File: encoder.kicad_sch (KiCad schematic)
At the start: 24 parts

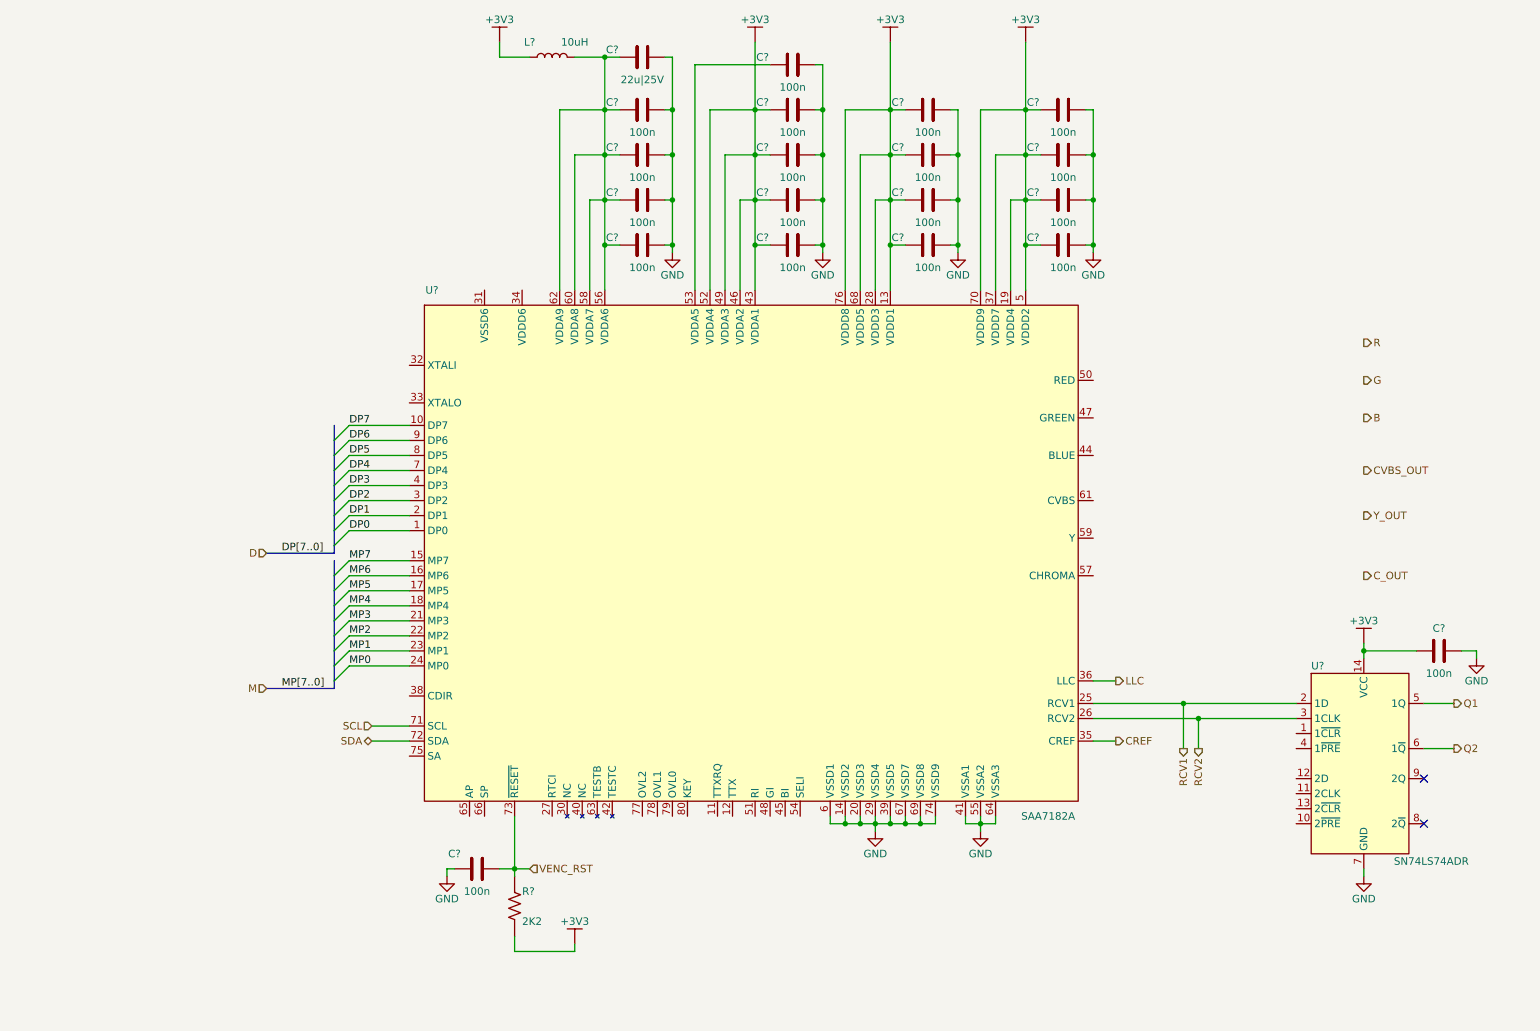
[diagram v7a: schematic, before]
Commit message: added connectors and crystal, osc
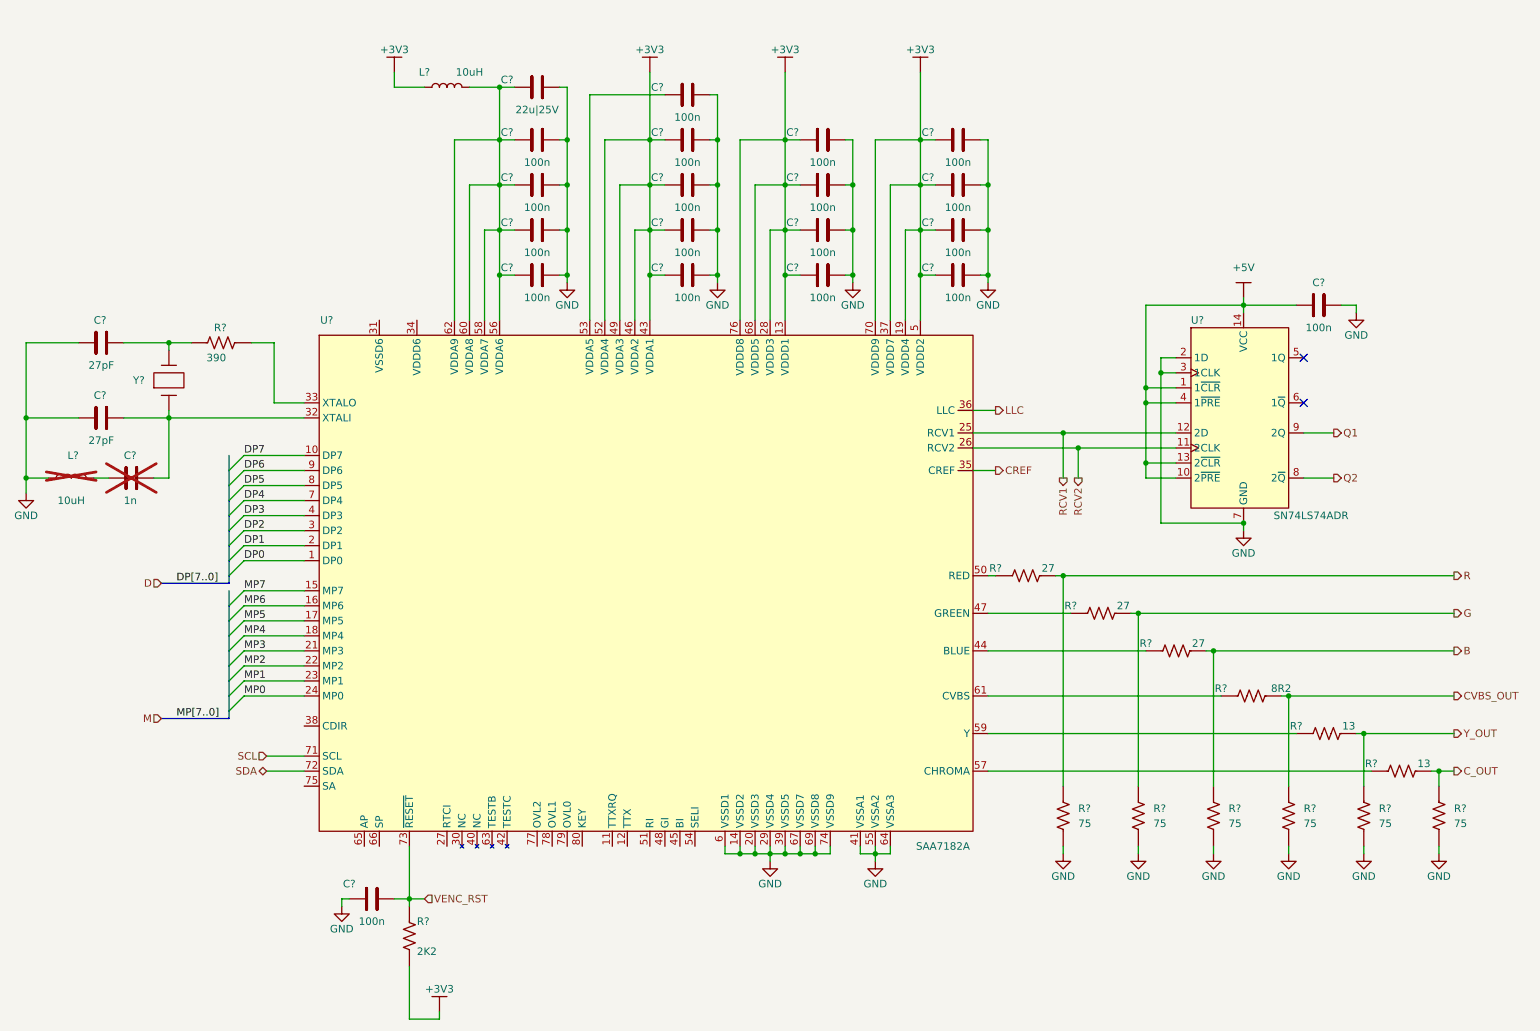
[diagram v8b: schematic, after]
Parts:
- added C?: 1n, symbol tbc:GCM1885C2A102FA16D
- added C? (x2): 27pF, symbol tbc:GCM1885C2A270JA16D
- added L?: 10uH, symbol tbc:LQM21DH100M70L
- added R? (x6): 75, symbol tbc:RC0603FR-0775RL
- added R? (x2): 13, symbol tbc:RC0603FR-0713RL
- added R? (x3): 27, symbol tbc:RC0603FR-0727RL
- added R?: 390, symbol tbc:RC0603FR-07390RL
- added R?: 8R2, symbol tbc:RC0603FR-078R2L
- added Y?: ABLS-27.000MHZ-B2F-T, symbol tbc:ABLS-27.000MHZ-B2F-T
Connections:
- net +3V3: no longer C?.1, U?.14 (VCC)
- net B: now also R?.2, R?.2
- net CVBS_OUT: now also R?.2, R?.2
- net C_OUT: now also R?.2, R?.2
- net G: now also R?.2, R?.2
- net GND: now also U?.2 (1D), U?.3 (1CLK), C?.2, C?.2, L?.1, R?.1, R?.1, R?.1, R?.1, R?.1, R?.1
- net Q1: now also U?.9 (2Q); no longer U?.5 (1Q)
- net Q2: now also U?.8 (2~{Q}); no longer U?.6 (1~{Q})
- net R: now also R?.2, R?.2
- net RCV1: now also U?.12 (2D); no longer U?.2 (1D)
- net RCV2: now also U?.11 (2CLK); no longer U?.3 (1CLK)
- net Y_OUT: now also R?.2, R?.2
- net +5V: now reaches U?.1 (1~{CLR})
- net +5V: now also C?.1, U?.10 (2~{PRE}), U?.13 (2~{CLR}), U?.14 (VCC), U?.4 (1~{PRE})
- net at U?.32 (XTALI): now also C?.1, C?.1, Y?.1
- net at U?.33 (XTALO): now also R?.1
- net at U?.44 (BLUE): now also R?.1
- net at U?.47 (GREEN): now also R?.1
- net at U?.50 (RED): now also R?.1
- net at U?.57 (CHROMA): now also R?.1
- net at U?.59 (Y): now also R?.1
- net at U?.61 (CVBS): now also R?.1
- new net: C?.1, R?.2, Y?.2
- new net: C?.2, L?.2
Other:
- moved on the sheet: C?, L?, R?, U?
